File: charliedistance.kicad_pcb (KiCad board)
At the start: 2 copper layers, 71.5 x 141.1 mm, 334 parts, among them IC1 SAMD21G18A, J1 USB_C, J2 DEBUG, Q1 CJ2302, Q2 CJ2305, Q3 MPT60363T, SW1 RESET, SW2 A, SW3 B, SW4 X, SW5 Y, U1 IS31FL3731-QF, U2 IS31FL3731-QF, U3 HX9193-33GB, U4 GD25Q32C, X1 Badgelife_sao_connector_v169b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

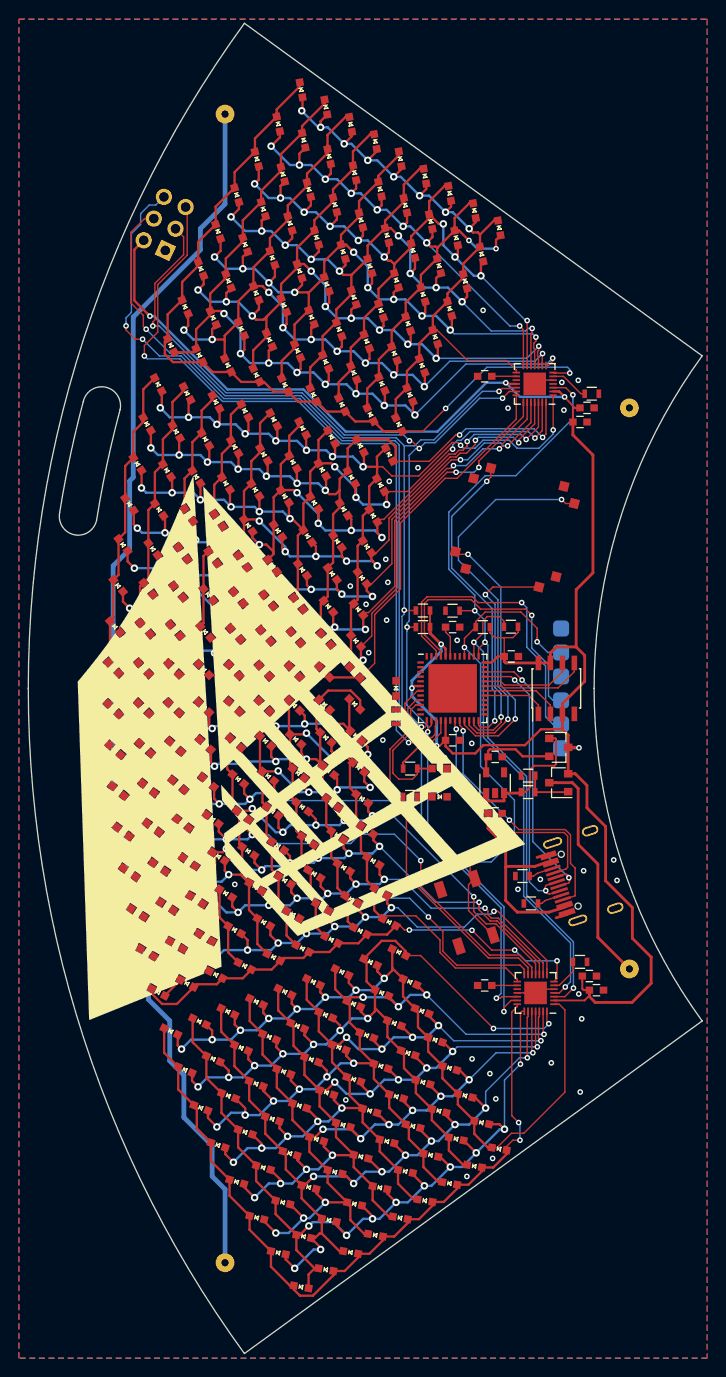
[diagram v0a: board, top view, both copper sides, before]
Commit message: Updates to production version
Changed infrared setup, added step-up for battery power, added battery power switch, added more capacitors, changed and added logos, etc.
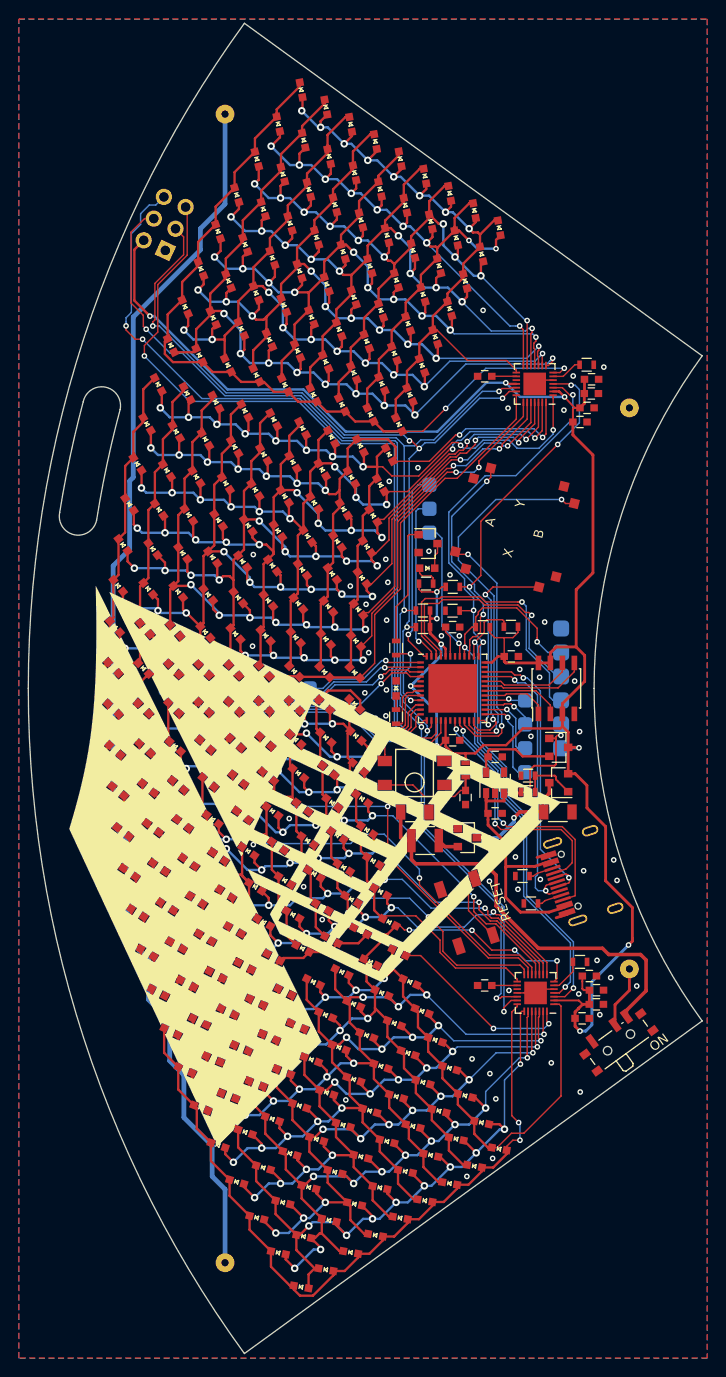
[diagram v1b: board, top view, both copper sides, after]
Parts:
- removed the G*** at (49.3, 67.6)
- added C12: 10uF, Capacitors_SMD:C_0603, F.Cu at (110.2, 133.5)
- added C13: 10uF, Capacitors_SMD:C_0603, F.Cu at (108.7, 135.0)
- added C14: 10uF, Capacitors_SMD:C_0603, F.Cu at (109.7, 68.7)
- added C15: 10uF, Capacitors_SMD:C_0603, F.Cu at (109.7, 67.2)
- added C16: 100uF, Capacitors_SMD:C_1206, F.Cu at (91.0, 113.1)
- added C17: 100uF, Capacitors_SMD:C_1206, F.Cu at (106.2, 113.1)
- added C18: 2.2uF, Capacitors_SMD:C_0603, F.Cu at (96.4, 111.6)
- added G***: LOGO, Aesthetics:bh2020_make_clean_silk, B.Cu at (72.2, 78.2)
- added G***: LOGO, Aesthetics:bh2020_logo_2_silk, F.Cu at (85.6, 99.7)
- added L1: 47uH, Inductors_SMD:L_1210, F.Cu at (92.1, 116.1)
- added R15: 1k, Resistors_SMD:R_0603, F.Cu at (89.0, 95.7)
- added R16: 100, Resistors_SMD:R_0603, F.Cu at (96.4, 108.7)
- added SW6: POWER, Buttons_Switches_SMD:SW_SPDT_PCM12, F.Cu at (112.4, 137.3)
- added TP1: PA0, Connectors:TestPoint_Large, B.Cu at (79.8, 100.0)
- added TP10: PA28, Connectors:TestPoint_Large, B.Cu at (92.5, 83.5)
- added TP11: PA19, Connectors:TestPoint_Large, B.Cu at (102.7, 101.3)
- added TP12: PA18, Connectors:TestPoint_Large, B.Cu at (102.7, 103.8)
- added TP13: PA17, Connectors:TestPoint_Large, B.Cu at (102.7, 106.3)
- added TP14: PA16, Connectors:TestPoint_Large, B.Cu at (102.7, 108.9)
- added TP2: PA1, Connectors:TestPoint_Large, B.Cu at (77.3, 100.0)
- added TP3: PA2, Connectors:TestPoint_Large, B.Cu at (74.8, 100.0)
- added TP4: PA3, Connectors:TestPoint_Large, B.Cu at (72.2, 100.0)
- added TP5: PB9, Connectors:TestPoint_Large, B.Cu at (69.7, 100.0)
- added TP6: PA6, Connectors:TestPoint_Large, B.Cu at (67.1, 100.0)
- added TP7: PA7, Connectors:TestPoint_Large, B.Cu at (64.6, 100.0)
- added TP8: PB3, Connectors:TestPoint_Large, B.Cu at (92.5, 78.4)
- added TP9: PB2, Connectors:TestPoint_Large, B.Cu at (92.5, 81.0)
- added U5: QX2304, TO_SOT_Packages_SMD:SOT-23, F.Cu at (96.5, 115.8)
- added U6: IRM-H6xxT, Opto:IRM-H6xxT, F.Cu at (91.0, 109.0)
- Q3: value MPT60363T -> BC817; footprint Opto:LED_0603_Clean -> TO_SOT_Packages_SMD:SOT-23
- R8: value R -> 100
- R9: value R -> 4.7k
- moved D290 24.3 mm to (92.3, 87.2)
- moved Q3 23.9 mm to (92.4, 84.6)
- moved R8 22.7 mm to (92.2, 88.9)
- moved R9 19.8 mm to (95.0, 89.2), turned to 180 degrees
- moved R2 3.12 mm to (109.2, 65.7)
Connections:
- net IS_INTB renamed INTB_1
- D290 pad 1: GND -> Net-(D290-Pad1)
- IC1 pad 39: Net-(IC1-Pad39) -> INTB_2
- J2 pad 2: /samd21/SWDIO -> /psu/USB_BUS_POWER
- J2 pad 3: /samd21/SWDCLK -> /samd21/SWDIO
- J2 pad 4: Net-(J2-Pad4) -> /samd21/SWDCLK
- Q2 pad 3: /psu/BAT+ -> Net-(C17-Pad1)
- Q3 pad 1: /samd21/IR_RX -> Net-(Q3-Pad1)
- R8 pad 1: /samd21/IR_TX -> VCC
- R9 pad 1: VCC -> INTB_2
- R9 pad 2: /samd21/IR_RX -> VCC
- U2 pad 4: /issi_charlie_9x16_b/~INTB -> INTB_2
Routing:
- net Net-(C16-Pad1): track 0.00 -> 44.0 mm
- net INTB_2: track 0.00 -> 38.6 mm, vias 0 -> 4
- net Net-(IC1-Pad12): track 0.00 -> 31.6 mm, vias 0 -> 1
- net Net-(IC1-Pad11): track 0.00 -> 29.0 mm, vias 0 -> 1
- net Net-(IC1-Pad8): track 0.00 -> 27.3 mm, vias 0 -> 1
- net Net-(IC1-Pad4): track 0.00 -> 22.0 mm, vias 0 -> 1
- net Net-(IC1-Pad48): track 0.00 -> 20.8 mm, vias 0 -> 1
- net Net-(IC1-Pad3): track 0.00 -> 19.4 mm, vias 0 -> 1
- net /psu/BAT+: track 24.7 -> 6.56 mm
- net Net-(IC1-Pad47): track 0.00 -> 17.8 mm, vias 0 -> 1
- net Net-(IC1-Pad2): track 0.00 -> 16.5 mm, vias 0 -> 1
- net Net-(IC1-Pad41): track 0.00 -> 14.9 mm, vias 0 -> 1
- net Net-(IC1-Pad1): track 0.00 -> 13.1 mm, vias 0 -> 1
- net Net-(Q3-Pad1): track 0.00 -> 12.8 mm
- net Net-(C17-Pad1): track 0.00 -> 11.8 mm, vias 0 -> 2
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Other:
- rule pad_to_mask_clearance: 0.051 -> 0.05
- rule solder_mask_min_width: 0.25 -> 0.1
- board text added: "2"
- board text added: "4"
- board text added: "5"
- board text added: "5ctvq7gjwg9khts4 r7uim39de3qupp9s"
- board text added: "6"
- board text added: "7"
- board text added: "9"
- board text added: "A"
- board text added: "B"
- board text added: "Badge design: @thomasflummer Get started at: https://github.com/bornhack/badge2020 #badgelife"
- board text added: "C"
- board text added: "D"
- board text added: "G"
- board text added: "ON"
- board text added: "R"
- board text added: "U"
- board text added: "V"
- board text added: "X"
- board text added: "Y"
- board text added: "a"
- board text added: "b"
- board text added: "c"
- board text added: "d"
- board text added: "e"
- board text added: "i"
- board text added: "o"
- board text added: "p"
- board text added: "q"
- board text added: "r"
- board text added: "s"
- board text added: "t"
- board text added: "u"
- board text added: "v"
- board text added: "w"
- board text added: "x"
- board text added: "y"
- board text removed: "#badgelife"
- board text removed: "BornHack Badge Prototype Design: @thomasflummer"
- board text removed: "GND"
- board text removed: "SWDCLK"
- board text removed: "SWDIO"
- board text removed: "VCC"
